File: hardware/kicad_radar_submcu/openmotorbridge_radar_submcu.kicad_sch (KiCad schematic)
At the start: 0 parts

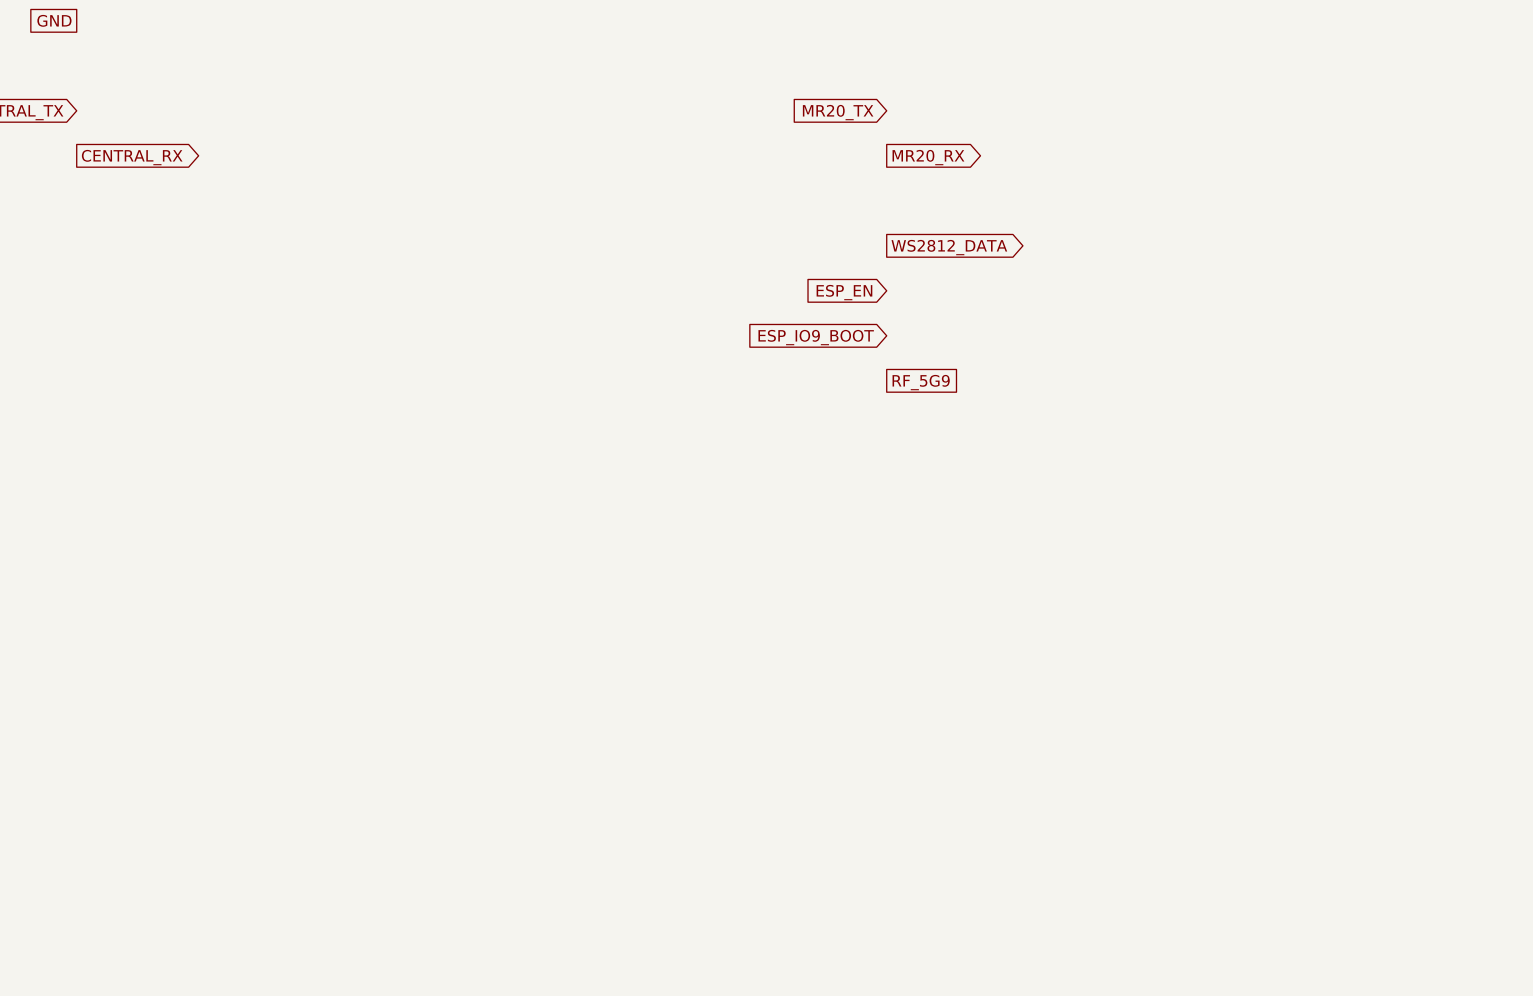
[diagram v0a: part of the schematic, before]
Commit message: feat(system): architecture refinement v6 across hardware, firmware and docs
- Hardware:
  * PCBA 09 (OMM 2.4 GHz Intercom): Upgrade to Everest Semi ES8388 stereo codec (QFN-28)
    and Multi-Use USB-C connector (J1) combining power, WebUSB flashing and stereo audio.
  * PCBA 08 (Radar 2.0 Sub-MCU): Strict HF hardening (2x U.FL: 6.5 GHz UWB & 5.9 GHz V2X;
    no 2.4 GHz/BLE at rear), right-angle 4-pin flashing header J3.
  * PCBA 03 (Cartridge): 8-pin Kelvin-grounded audio/power header with isolated PGND/AGND.
  * CAD: Standardize DIN 934 hex nut pockets across module enclosures.

- Firmware:
  * UWB Backbone: Add multi-channel substream audio downlink (sub-channels 0/1 music,
    sub-channel 2 voice) and audio uplink packet definitions.
  * Smart Cartridge: Implement zero-latency (<1 ms) voice routing to intercom mic pin,
    A2DP music stream buffering for mesh group sharing, and 100 Hz upstream audio capture.
  * Central Box: Central DSP mixer ducking (-18 dB), voice activity detection (VAD), and
    multi-channel UWB dispatching.
  * OMM Module: Implement ES8388 stereo codec driver and I2S master duplex stream.
  * Radar Sub-MCU: Confirm 2.4 GHz RF disable and autonomous emergency strobe trigger (<1 ms).

- Documentation & WebApp:
  * Align DE & EN chapters (01, 02, 03, 04b, 07, 08, 14, 15, 16) with v6 specifications.
  * Update WebApp PWA System Builder with ES8388 stereo codec and OMM 446 PMR/DMR module.
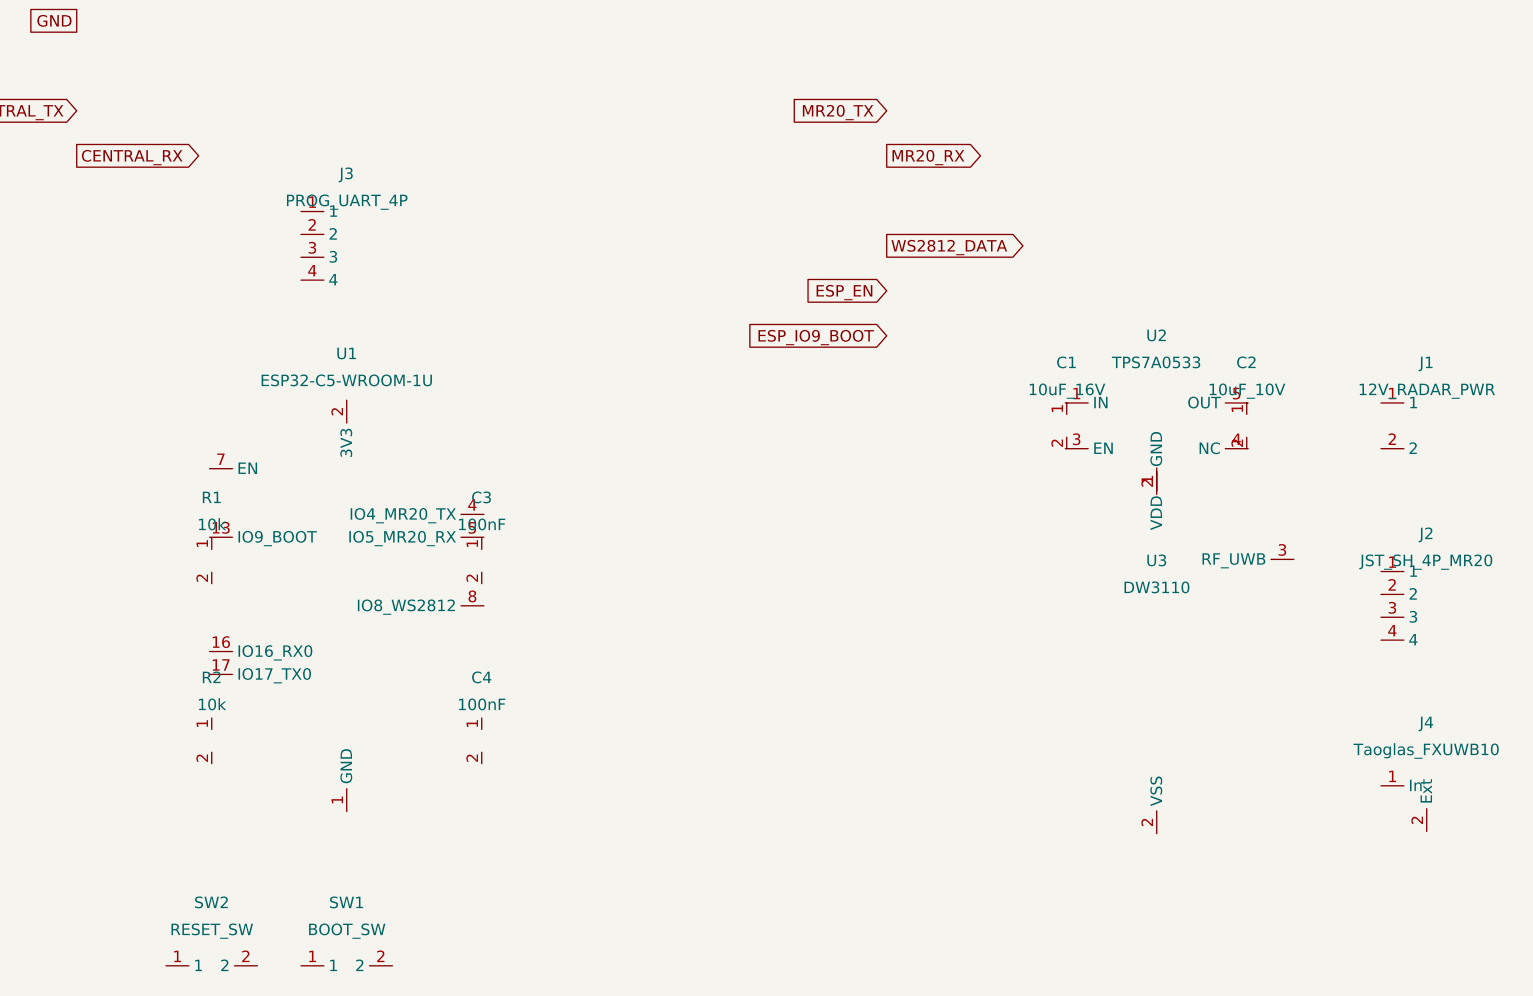
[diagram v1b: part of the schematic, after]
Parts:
- added C1: 10uF_16V, Capacitor_SMD:C_0805_2012Metric, symbol Device:C_Small
- added C2: 10uF_10V, Capacitor_SMD:C_0805_2012Metric, symbol Device:C_Small
- added C3, C4: 100nF, Capacitor_SMD:C_0603_1608Metric, symbol Device:C_Small
- added J1: 12V_RADAR_PWR, Connector_JST:JST_JWPF_B02B-JWPF-SK-R_1x02_P2.00mm_Vertical, symbol Connector:Conn_01x02
- added J2: JST_SH_4P_MR20, Connector_JST:JST_SH_SM04B-SRSS-TB_1x04-1MP_P1.00mm_Horizontal, symbol Connector:Conn_01x04
- added J3: PROG_UART_4P, Connector_PinHeader_2.54mm:PinHeader_1x04_P2.54mm_Horizontal, symbol Connector:Conn_01x04
- added J4: Taoglas_FXUWB10, Connector_Coaxial:U.FL_Hirose_U.FL-R-SMT-1_Vertical, symbol Connector:Conn_Coaxial
- added R1, R2: 10k, Resistor_SMD:R_0603_1608Metric, symbol Device:R_Small
- added SW1: BOOT_SW, Button_Switch_SMD:SW_Push_SPST_NO_Alps_SKRK, symbol Switch:SW_Push
- added SW2: RESET_SW, Button_Switch_SMD:SW_Push_SPST_NO_Alps_SKRK, symbol Switch:SW_Push
- added U1: ESP32-C5-WROOM-1U, RF_Module:ESP32-C3-WROOM-02U, symbol RF_Module:ESP32-C5-WROOM-1U
- added U2: TPS7A0533, Package_TO_SOT_SMD:SOT-23-5, symbol Regulator_Linear:TPS7A0533
- added U3: DW3110, RF_Module:DW3110, symbol RF_Module:DW3110
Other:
- title: OpenMotorBridge Radar 2.0 Sub-MCU, 5.9 GHz V2X & LED Halo (PCBA 08) -> OpenMotorBridge Radar 2.0 Sub-MCU, UWB & LED Halo (PCBA 08)
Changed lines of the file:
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@@
 (kicad_sch
-	(version 20240108)
-	(generator "openmotorbridge_gen")
+	(version 20260306)
+	(generator "eeschema")
 	(generator_version "10.0")
 	(paper "A3")
 	(title_block
-		(title "OpenMotorBridge Radar 2.0 Sub-MCU, 5.9 GHz V2X & LED Halo (PCBA 08)")
-		(date "2026-09-23")
+		(title "OpenMotorBridge Radar 2.0 Sub-MCU, UWB & LED Halo (PCBA 08)")
+		(date "2026-10-07")
 		(rev "v2.0-wing")
 		(company "OpenMotorBridge Open Source Hardware")
-		(comment 1 "ESP32-C5 Sub-MCU (ITS-G5 5.9 GHz Sniffer), Wheeltec MR20 Adapter, 36-LED Matrix")
+		(comment 1 "ESP32-C5 Sub-MCU, Qorvo DW3110 UWB Transceiver, Wheeltec MR20 Adapter, 36-LED Halo")
+		(comment 2 "J3 4-Pin 90° Flash/Debug Header (3V3, TX, RX, GND) - Onboard U.FL on ESP32-C5")
 	)
 	(global_label "VCC_5V" (shape input) (at 30.0 30.0 180) (effects (font (size 1.27 1.27)) (justify right)))
@@
 	(global_label "ESP_EN" (shape input) (at 120.0 65.0 180) (effects (font (size 1.27 1.27)) (justify right)))
 	(global_label "ESP_IO9_BOOT" (shape input) (at 120.0 70.0 180) (effects (font (size 1.27 1.27)) (justify right)))
-	(global_label "RF_5G9" (shape passive) (at 120.0 75.0 0) (effects (font (size 1.27 1.27)) (justify left)))
+	(symbol (lib_id "RF_Module:ESP32-C5-WROOM-1U") (at 60.0 100.0 0) (unit 1)
+		(in_bom yes) (on_board yes) (dnp no)
+		(property "Reference" "U1" (at 60.0 72.0 0) (effects (font (size 1.27 1.27))))
+		(property "Value" "ESP32-C5-WROOM-1U" (at 60.0 75.0 0) (effects (font (size 1.27 1.27))))
+		(property "Footprint" "RF_Module:ESP32-C3-WROOM-02U" (at 0 0 0) (effects (font (size 1.27 1.27)) hide))
+		(pin "1")
+		(pin "2")
+		(pin "7")
+		(pin "4")
+		(pin "5")
+		(pin "8")
+		(pin "13")
+		(pin "16")
+		(pin "17")
+	)
+	(symbol (lib_id "Regulator_Linear:TPS7A0533") (at 150.0 80.0 0) (unit 1)
+		(in_bom yes) (on_board yes) (dnp no)
+		(property "Reference" "U2" (at 150.0 70.0 0) (effects (font (size 1.27 1.27))))
+		(property "Value" "TPS7A0533" (at 150.0 73.0 0) (effects (font (size 1.27 1.27))))
+		(property "Footprint" "Package_TO_SOT_SMD:SOT-23-5" (at 0 0 0) (effects (font (size 1.27 1.27)) hide))
+		(pin "1")
+		(pin "2")
+		(pin "3")
+		(pin "4")
+		(pin "5")
+	)
+	(symbol (lib_id "RF_Module:DW3110") (at 150.0 105.0 0) (unit 1)
+		(in_bom yes) (on_board yes) (dnp no)
+		(property "Reference" "U3" (at 150.0 95.0 0) (effects (font (size 1.27 1.27))))
+		(property "Value" "DW3110" (at 150.0 98.0 0) (effects (font (size 1.27 1.27))))
+		(property "Footprint" "RF_Module:DW3110" (at 0 0 0) (effects (font (size 1.27 1.27)) hide))
+		(pin "1")
+		(pin "2")
+		(pin "3")
+	)
+	(symbol (lib_id "Connector:Conn_01x02") (at 180.0 80.0 0) (unit 1)
+		(in_bom yes) (on_board yes) (dnp no)
+		(property "Reference" "J1" (at 180.0 73.0 0) (effects (font (size 1.27 1.27))))
+		(property "Value" "12V_RADAR_PWR" (at 180.0 76.0 0) (effects (font (size 1.27 1.27))))
+		(property "Footprint" "Connector_JST:JST_JWPF_B02B-JWPF-SK-R_1x02_P2.00mm_Vertical" (at 0 0 0) (effects (font (size 1.27 1.27)) hide))
+		(pin "1")
+		(pin "2")
+	)
+	(symbol (lib_id "Connector:Conn_01x04") (at 180.0 100.0 0) (unit 1)
+		(in_bom yes) (on_board yes) (dnp no)
+		(property "Reference" "J2" (at 180.0 92.0 0) (effects (font (size 1.27 1.27))))
+		(property "Value" "JST_SH_4P_MR20" (at 180.0 95.0 0) (effects (font (size 1.27 1.27))))
+		(property "Footprint" "Connector_JST:JST_SH_SM04B-SRSS-TB_1x04-1MP_P1.00mm_Horizontal" (at 0 0 0) (effects (font (size 1.27 1.27)) hide))
+		(pin "1")
+		(pin "2")
+		(pin "3")
+		(pin "4")
+	)
+	(symbol (lib_id "Connector:Conn_01x04") (at 60.0 60.0 0) (unit 1)
+		(in_bom yes) (on_board yes) (dnp no)
+		(property "Reference" "J3" (at 60.0 52.0 0) (effects (font (size 1.27 1.27))))
+		(property "Value" "PROG_UART_4P" (at 60.0 55.0 0) (effects (font (size 1.27 1.27))))
+		(property "Footprint" "Connector_PinHeader_2.54mm:PinHeader_1x04_P2.54mm_Horizontal" (at 0 0 0) (effects (font (size 1.27 1.27)) hide))
+		(pin "1")
+		(pin "2")
+		(pin "3")
+		(pin "4")
+	)
+	(symbol (lib_id "Connector:Conn_Coaxial") (at 180.0 120.0 0) (unit 1)
+		(in_bom yes) (on_board yes) (dnp no)
+		(property "Reference" "J4" (at 180.0 113.0 0) (effects (font (size 1.27 1.27))))
+		(property "Value" "Taoglas_FXUWB10" (at 180.0 116.0 0) (effects (font (size 1.27 1.27))))
+		(property "Footprint" "Connector_Coaxial:U.FL_Hirose_U.FL-R-SMT-1_Vertical" (at 0 0 0) (effects (font (size 1.27 1.27)) hide))
+		(pin "1")
+		(pin "2")
+	)
+	(symbol (lib_id "Switch:SW_Push") (at 60.0 140.0 0) (unit 1)
+		(in_bom yes) (on_board yes) (dnp no)
+		(property "Reference" "SW1" (at 60.0 133.0 0) (effects (font (size 1.27 1.27))))
+		(property "Value" "BOOT_SW" (at 60.0 136.0 0) (effects (font (size 1.27 1.27))))
+		(property "Footprint" "Button_Switch_SMD:SW_Push_SPST_NO_Alps_SKRK" (at 0 0 0) (effects (font (size 1.27 1.27)) hide))
+		(pin "1")
+		(pin "2")
+	)
+	(symbol (lib_id "Switch:SW_Push") (at 45.0 140.0 0) (unit 1)
+		(in_bom yes) (on_board yes) (dnp no)
+		(property "Reference" "SW2" (at 45.0 133.0 0) (effects (font (size 1.27 1.27))))
+		(property "Value" "RESET_SW" (at 45.0 136.0 0) (effects (font (size 1.27 1.27))))
+		(property "Footprint" "Button_Switch_SMD:SW_Push_SPST_NO_Alps_SKRK" (at 0 0 0) (effects (font (size 1.27 1.27)) hide))
+		(pin "1")
+		(pin "2")
+	)
+	(symbol (lib_id "Device:C_Small") (at 140.0 80.0 0) (unit 1)
+		(in_bom yes) (on_board yes) (dnp no)
+		(property "Reference" "C1" (at 140.0 73.0 0) (effects (font (size 1.27 1.27))))
+		(property "Value" "10uF_16V" (at 140.0 76.0 0) (effects (font (size 1.27 1.27))))
+		(property "Footprint" "Capacitor_SMD:C_0805_2012Metric" (at 0 0 0) (effects (font (size 1.27 1.27)) hide))
+		(pin "1")
+		(pin "2")
+	)
+	(symbol (lib_id "Device:C_Small") (at 160.0 80.0 0) (unit 1)
+		(in_bom yes) (on_board yes) (dnp no)
+		(property "Reference" "C2" (at 160.0 73.0 0) (effects (font (size 1.27 1.27))))
+		(property "Value" "10uF_10V" (at 160.0 76.0 0) (effects (font (size 1.27 1.27))))
+		(property "Footprint" "Capacitor_SMD:C_0805_2012Metric" (at 0 0 0) (effects (font (size 1.27 1.27)) hide))
+		(pin "1")
+		(pin "2")
+	)
+	(symbol (lib_id "Device:C_Small") (at 75.0 95.0 0) (unit 1)
+		(in_bom yes) (on_board yes) (dnp no)
+		(property "Reference" "C3" (at 75.0 88.0 0) (effects (font (size 1.27 1.27))))
+		(property "Value" "100nF" (at 75.0 91.0 0) (effects (font (size 1.27 1.27))))
+		(property "Footprint" "Capacitor_SMD:C_0603_1608Metric" (at 0 0 0) (effects (font (size 1.27 1.27)) hide))
+		(pin "1")
+		(pin "2")
+	)
+	(symbol (lib_id "Device:C_Small") (at 75.0 115.0 0) (unit 1)
+		(in_bom yes) (on_board yes) (dnp no)
+		(property "Reference" "C4" (at 75.0 108.0 0) (effects (font (size 1.27 1.27))))
+		(property "Value" "100nF" (at 75.0 111.0 0) (effects (font (size 1.27 1.27))))
+		(property "Footprint" "Capacitor_SMD:C_0603_1608Metric" (at 0 0 0) (effects (font (size 1.27 1.27)) hide))
+		(pin "1")
+		(pin "2")
+	)
+	(symbol (lib_id "Device:R_Small") (at 45.0 95.0 0) (unit 1)
+		(in_bom yes) (on_board yes) (dnp no)
+		(property "Reference" "R1" (at 45.0 88.0 0) (effects (font (size 1.27 1.27))))
+		(property "Value" "10k" (at 45.0 91.0 0) (effects (font (size 1.27 1.27))))
+		(property "Footprint" "Resistor_SMD:R_0603_1608Metric" (at 0 0 0) (effects (font (size 1.27 1.27)) hide))
+		(pin "1")
+		(pin "2")
+	)
+	(symbol (lib_id "Device:R_Small") (at 45.0 115.0 0) (unit 1)
+		(in_bom yes) (on_board yes) (dnp no)
+		(property "Reference" "R2" (at 45.0 108.0 0) (effects (font (size 1.27 1.27))))
+		(property "Value" "10k" (at 45.0 111.0 0) (effects (font (size 1.27 1.27))))
+		(property "Footprint" "Resistor_SMD:R_0603_1608Metric" (at 0 0 0) (effects (font (size 1.27 1.27)) hide))
+		(pin "1")
+		(pin "2")
+	)
 )
